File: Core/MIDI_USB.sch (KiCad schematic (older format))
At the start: 27 parts, among them J1 Conn_01x04, J4 Conn_01x06, SW1 SW_Push_DPDT, U1 ATSAMD21G17D-A, U10 TLE9250V, U9 MCP2517FD-xSL, Y1 20MHz

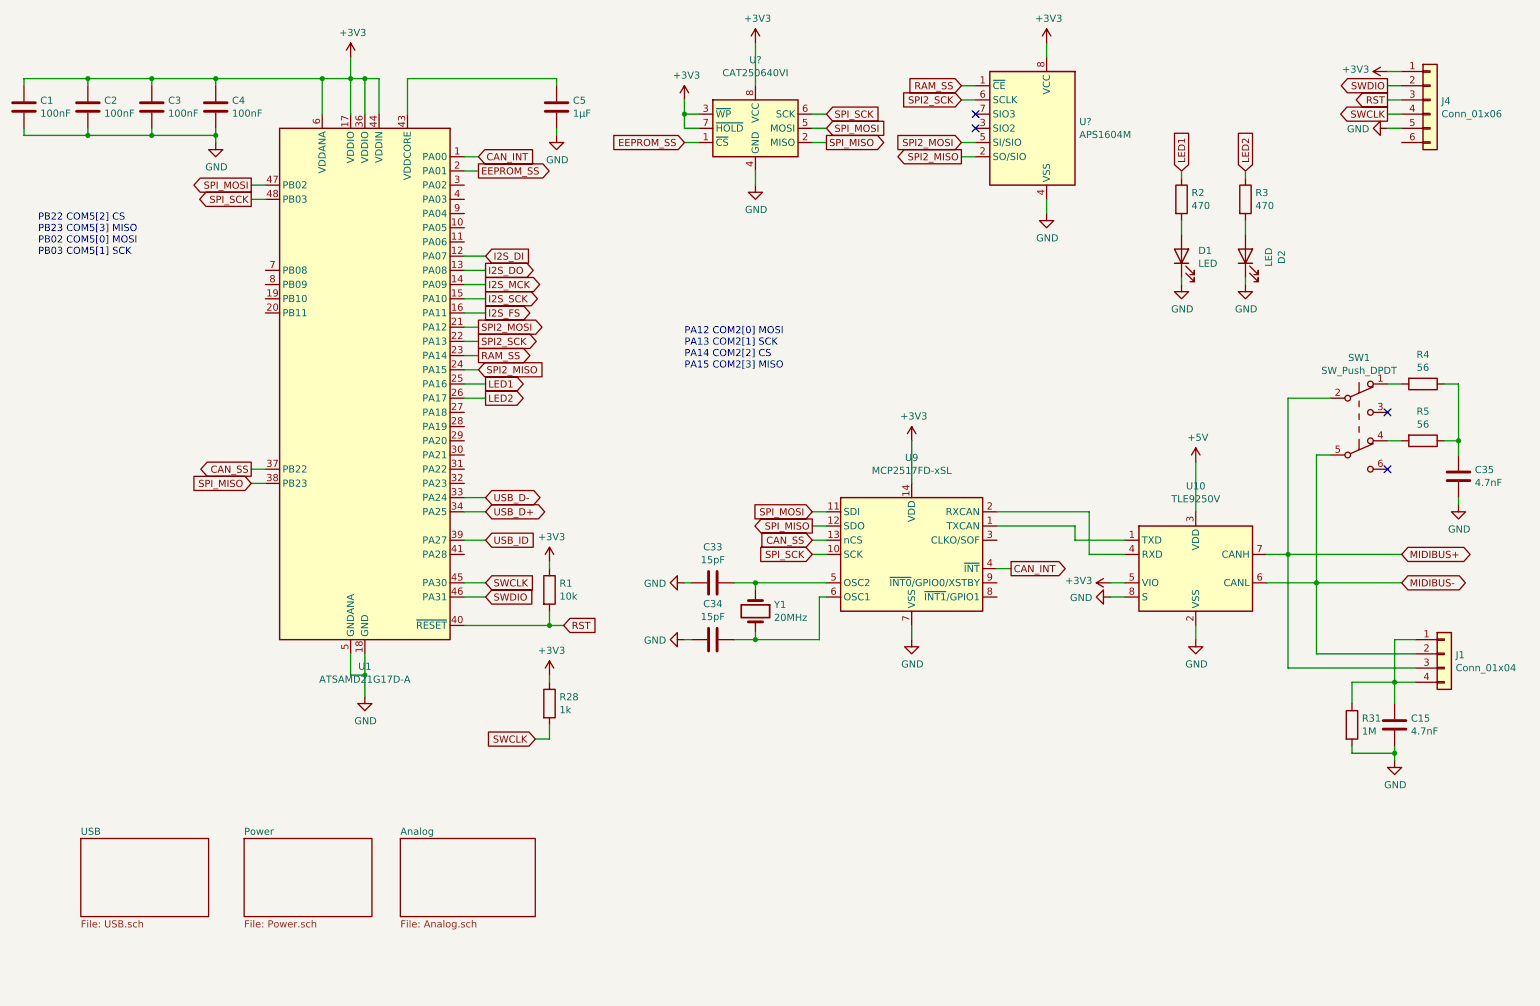
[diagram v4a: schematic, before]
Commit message: Add IO and bootloader buttons
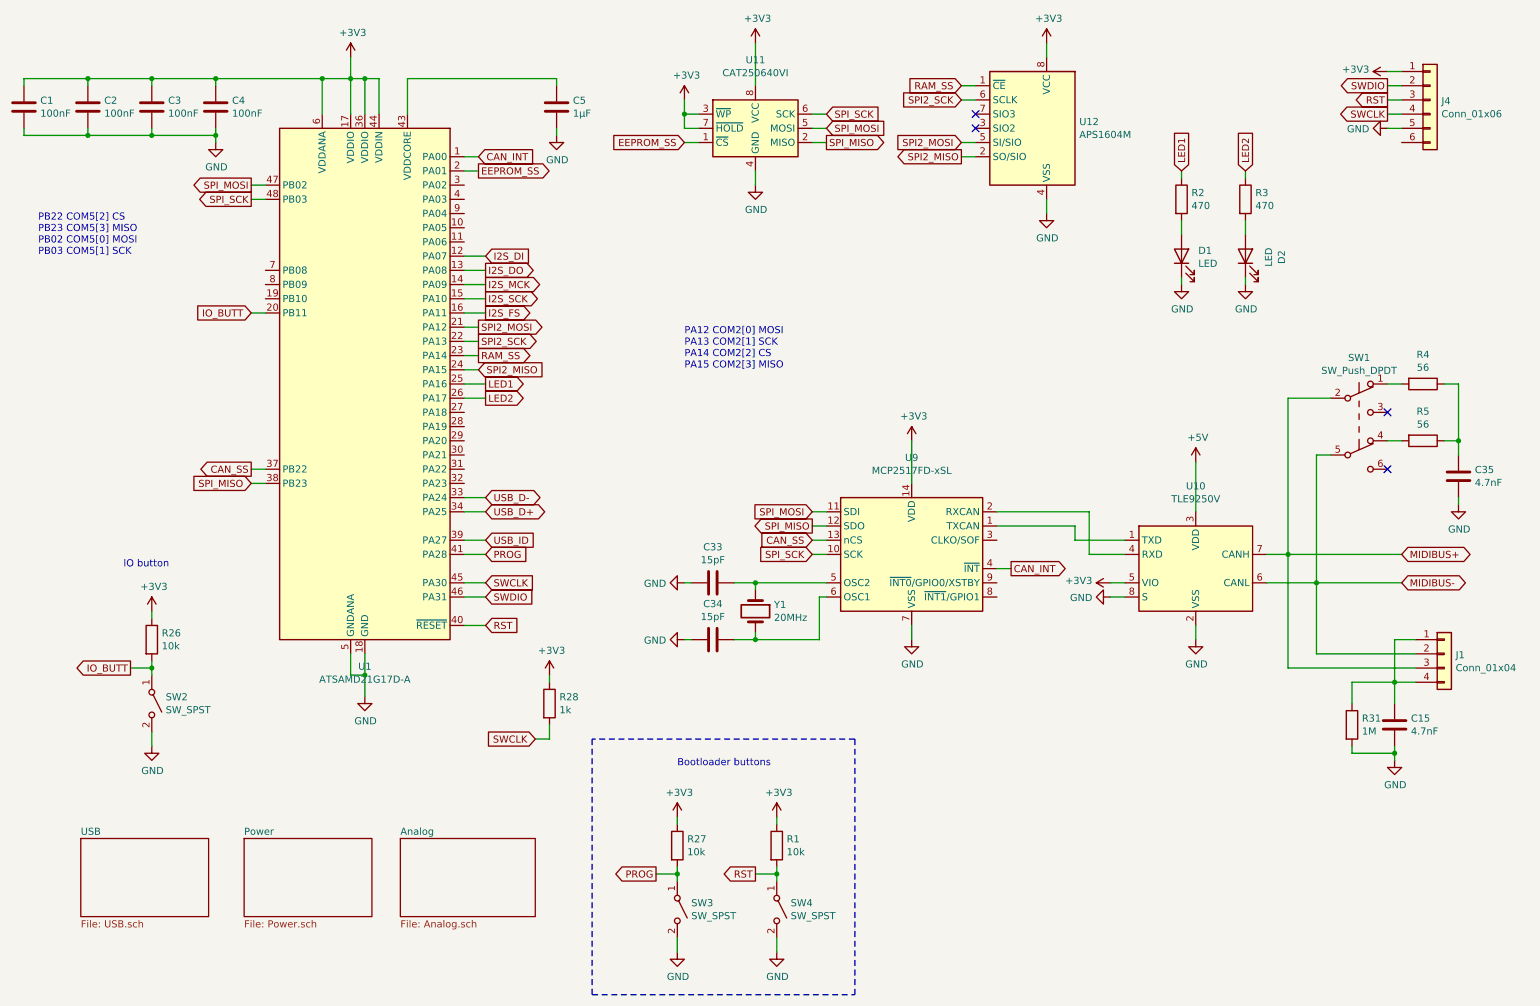
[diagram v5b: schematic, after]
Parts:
- added R26, R27: 10k, Resistor_SMD:R_0603_1608Metric, symbol Device:R
- added SW2: SW_SPST, Button_Switch_THT:SW_Tactile_SPST_Angled_PTS645Vx58-2LFS, symbol Switch:SW_SPST
- added SW3, SW4: SW_SPST, Button_Switch_SMD:SW_SPST_EVQP7C, symbol Switch:SW_SPST
- gave numbers to parts that had none: 2
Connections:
- net +3V3: now also R26.1, R27.1
- net GND: now also SW2.2 (B), SW3.2 (B), SW4.2 (B)
- net RST: now also SW4.1 (A)
- net IO_BUTT: now reaches U1.20 (PB11)
- net IO_BUTT: now also R26.2, SW2.1 (A)
- net PROG: now reaches U1.41 (PA28)
- net PROG: now also R27.2, SW3.1 (A)
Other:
- note added: "Bootloader buttons"
- note added: "IO button"
- moved on the sheet: R1
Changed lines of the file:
@@
 L Device:R R1
 U 1 1 60AB5ED7
-P 4300 4650
-F 0 "R1" H 4370 4696 50  0000 L CNN
-F 1 "10k" H 4370 4605 50  0000 L CNN
-F 2 "Resistor_SMD:R_0603_1608Metric" V 4230 4650 50  0001 C CNN
-F 3 "~" H 4300 4650 50  0001 C CNN
-	1    4300 4650
-	1    0    0    -1
-$EndComp
-Text GLabel 4400 4900 2    50   Input ~ 0
+P 5900 6450
+F 0 "R1" H 5970 6496 50  0000 L CNN
+F 1 "10k" H 5970 6405 50  0000 L CNN
+F 2 "Resistor_SMD:R_0603_1608Metric" V 5830 6450 50  0001 C CNN
+F 3 "~" H 5900 6450 50  0001 C CNN
+	1    5900 6450
+	1    0    0    -1
+$EndComp
+Text GLabel 3850 4900 2    50   Input ~ 0
 RST
 Wire Wire Line
-	4400 4900 4300 4900
-Wire Wire Line
-	4300 4800 4300 4900
-Connection ~ 4300 4900
-Wire Wire Line
-	4300 4900 3700 4900
-Wire Wire Line
-	4300 4500 4300 4450
+	3850 4900 3700 4900
+Wire Wire Line
+	5900 6600 5900 6650
+Wire Wire Line
+	5900 6300 5900 6250
 $Comp
 L power:+3V3 #PWR0110
 U 1 1 60ABC9C1
-P 4300 4450
-F 0 "#PWR0110" H 4300 4300 50  0001 C CNN
-F 1 "+3V3" H 4315 4623 50  0000 C CNN
-F 2 "" H 4300 4450 50  0001 C CNN
-F 3 "" H 4300 4450 50  0001 C CNN
-	1    4300 4450
+P 5900 6250
+F 0 "#PWR0110" H 5900 6100 50  0001 C CNN
+F 1 "+3V3" H 5915 6423 50  0000 C CNN
+F 2 "" H 5900 6250 50  0001 C CNN
+F 3 "" H 5900 6250 50  0001 C CNN
+	1    5900 6250
 	1    0    0    -1
 $EndComp
@@
 SWCLK
 $Comp
-L Memory_EEPROM:CAT250xxx U?
+L Memory_EEPROM:CAT250xxx U11
 U 1 1 62CF50E4
 P 5750 1400
-F 0 "U?" H 5750 1881 50  0000 C CNN
+F 0 "U11" H 5750 1881 50  0000 C CNN
 F 1 "CAT250640VI" H 5750 1790 50  0000 C CNN
 F 2 "Package_SO:SOIC-8_3.9x4.9mm_P1.27mm" H 5750 1400 50  0001 C CNN
@@
 $EndComp
 $Comp
-L Memory_RAM:ESP-PSRAM32 U?
+L Memory_RAM:ESP-PSRAM32 U12
 U 1 1 62CFA564
 P 7700 1400
-F 0 "U?" H 7370 1446 50  0000 R CNN
+F 0 "U12" H 7370 1446 50  0000 R CNN
 F 1 "APS1604M" H 7370 1355 50  0000 R CNN
 F 2 "Package_SO:SOIC-8_3.9x4.9mm_P1.27mm" H 7700 800 50  0001 C CNN
@@
 $EndComp
 $Comp
-L power:+3V3 #PWR?
+L power:+3V3 #PWR0138
 U 1 1 62D0BAED
 P 7800 800
-F 0 "#PWR?" H 7800 650 50  0001 C CNN
+F 0 "#PWR0138" H 7800 650 50  0001 C CNN
 F 1 "+3V3" H 7815 973 50  0000 C CNN
 F 2 "" H 7800 800 50  0001 C CNN
@@
 $EndComp
 $Comp
-L power:+3V3 #PWR?
+L power:+3V3 #PWR0163
 U 1 1 62D0BCD9
 P 5750 800
-F 0 "#PWR?" H 5750 650 50  0001 C CNN
+F 0 "#PWR0163" H 5750 650 50  0001 C CNN
 F 1 "+3V3" H 5765 973 50  0000 C CNN
 F 2 "" H 5750 800 50  0001 C CNN
@@
 	5750 1800 5750 1700
 $Comp
-L power:GND #PWR?
+L power:GND #PWR0165
 U 1 1 62D21FFD
 P 5750 1800
-F 0 "#PWR?" H 5750 1550 50  0001 C CNN
+F 0 "#PWR0165" H 5750 1550 50  0001 C CNN
 F 1 "GND" H 5755 1627 50  0000 C CNN
 F 2 "" H 5750 1800 50  0001 C CNN
@@
 $EndComp
 $Comp
-L power:GND #PWR?
+L power:GND #PWR0196
 U 1 1 62D228FF
 P 7800 2000
-F 0 "#PWR?" H 7800 1750 50  0001 C CNN
+F 0 "#PWR0196" H 7800 1750 50  0001 C CNN
 F 1 "GND" H 7805 1827 50  0000 C CNN
 F 2 "" H 7800 2000 50  0001 C CNN
@@
 	7200 1100 7300 1100
 $Comp
-L power:+3V3 #PWR?
+L power:+3V3 #PWR0197
 U 1 1 62D75718
 P 5250 1200
-F 0 "#PWR?" H 5250 1050 50  0001 C CNN
+F 0 "#PWR0197" H 5250 1050 50  0001 C CNN
 F 1 "+3V3" H 5265 1373 50  0000 C CNN
 F 2 "" H 5250 1200 50  0001 C CNN
@@
 Text Notes 5250 3100 0    50   ~ 0
 PA12 COM2[0] MOSI\nPA13 COM2[1] SCK\nPA14 COM2[2] CS\nPA15 COM2[3] MISO
+$Comp
+L Device:R R27
+U 1 1 62DDAB41
+P 5200 6450
+F 0 "R27" H 5270 6496 50  0000 L CNN
+F 1 "10k" H 5270 6405 50  0000 L CNN
+F 2 "Resistor_SMD:R_0603_1608Metric" V 5130 6450 50  0001 C CNN
+F 3 "~" H 5200 6450 50  0001 C CNN
+	1    5200 6450
+	1    0    0    -1
+$EndComp
+Wire Wire Line
+	5200 6600 5200 6650
+Wire Wire Line
+	5200 6300 5200 6250
+$Comp
+L power:+3V3 #PWR0206
+U 1 1 62DDAF8B
+P 5200 6250
+F 0 "#PWR0206" H 5200 6100 50  0001 C CNN
+F 1 "+3V3" H 5215 6423 50  0000 C CNN
+F 2 "" H 5200 6250 50  0001 C CNN
+F 3 "" H 5200 6250 50  0001 C CNN
+	1    5200 6250
+	1    0    0    -1
+$EndComp
+Text GLabel 3850 4400 2    50   Input ~ 0
+PROG
+Wire Wire Line
+	3850 4400 3700 4400
+$Comp
+L Switch:SW_SPST SW3
+U 1 1 62E052F7
+P 5200 6900
+F 0 "SW3" V 5154 6998 50  0000 L CNN
+F 1 "SW_SPST" V 5245 6998 50  0000 L CNN
+F 2 "Button_Switch_SMD:SW_SPST_EVQP7C" H 5200 6900 50  0001 C CNN
+F 3 "~" H 5200 6900 50  0001 C CNN
+	1    5200 6900
+	0    1    1    0
+$EndComp
+$Comp
+L Switch:SW_SPST SW4
+U 1 1 62E06963
+P 5900 6900
+F 0 "SW4" V 5854 6998 50  0000 L CNN
+F 1 "SW_SPST" V 5945 6998 50  0000 L CNN
+F 2 "Button_Switch_SMD:SW_SPST_EVQP7C" H 5900 6900 50  0001 C CNN
+F 3 "~" H 5900 6900 50  0001 C CNN
+	1    5900 6900
+	0    1    1    0
+$EndComp
+Text GLabel 5750 6650 0    50   Output ~ 0
+RST
+Text GLabel 5050 6650 0    50   Output ~ 0
+PROG
+Wire Wire Line
+	5050 6650 5200 6650
+Connection ~ 5200 6650
+Wire Wire Line
+	5200 6650 5200 6700
+Wire Wire Line
+	5750 6650 5900 6650
+Connection ~ 5900 6650
+Wire Wire Line
+	5900 6650 5900 6700
+Wire Wire Line
+	5900 7200 5900 7100
+Wire Wire Line
+	5200 7200 5200 7100
+$Comp
+L power:GND #PWR0207
+U 1 1 62E213B4
+P 5900 7200
+F 0 "#PWR0207" H 5900 6950 50  0001 C CNN
+F 1 "GND" H 5905 7027 50  0000 C CNN
+F 2 "" H 5900 7200 50  0001 C CNN
+F 3 "" H 5900 7200 50  0001 C CNN
+	1    5900 7200
+	1    0    0    -1
+$EndComp
+$Comp
+L power:GND #PWR0208
+U 1 1 62E2221F
+P 5200 7200
+F 0 "#PWR0208" H 5200 6950 50  0001 C CNN
+F 1 "GND" H 5205 7027 50  0000 C CNN
+F 2 "" H 5200 7200 50  0001 C CNN
+F 3 "" H 5200 7200 50  0001 C CNN
+	1    5200 7200
+	1    0    0    -1
+$EndComp
+Text Notes 5200 5900 0    50   ~ 0
+Bootloader buttons
+Wire Notes Line
+	6450 7500 6450 5700
+Wire Notes Line
+	6450 5700 4600 5700
+Wire Notes Line
+	4600 5700 4600 7500
+Wire Notes Line
+	4600 7500 6450 7500
+$Comp
+L Device:R R26
+U 1 1 62E3FA14
+P 1500 5000
+F 0 "R26" H 1570 5046 50  0000 L CNN
+F 1 "10k" H 1570 4955 50  0000 L CNN
+F 2 "Resistor_SMD:R_0603_1608Metric" V 1430 5000 50  0001 C CNN
+F 3 "~" H 1500 5000 50  0001 C CNN
+	1    1500 5000
+	1    0    0    -1
+$EndComp
+Wire Wire Line
+	1500 5150 1500 5200
+Wire Wire Line
+	1500 4850 1500 4800
+$Comp
+L power:+3V3 #PWR0209
+U 1 1 62E3FEC0
+P 1500 4800
+F 0 "#PWR0209" H 1500 4650 50  0001 C CNN
+F 1 "+3V3" H 1515 4973 50  0000 C CNN
+F 2 "" H 1500 4800 50  0001 C CNN
+F 3 "" H 1500 4800 50  0001 C CNN
+	1    1500 4800
+	1    0    0    -1
+$EndComp
+$Comp
+L Switch:SW_SPST SW2
+U 1 1 62E3FECA
+P 1500 5450
+F 0 "SW2" V 1454 5548 50  0000 L CNN
+F 1 "SW_SPST" V 1545 5548 50  0000 L CNN
+F 2 "Button_Switch_THT:SW_Tactile_SPST_Angled_PTS645Vx58-2LFS" H 1500 5450 50  0001 C CNN
+F 3 "~" H 1500 5450 50  0001 C CNN
+	1    1500 5450
+	0    1    1    0
+$EndComp
+Wire Wire Line
+	1350 5200 1500 5200
+Connection ~ 1500 5200
+Wire Wire Line
+	1500 5200 1500 5250
+Wire Wire Line
+	1500 5750 1500 5650
+$Comp
+L power:GND #PWR0210
+U 1 1 62E3FED8
+P 1500 5750
+F 0 "#PWR0210" H 1500 5500 50  0001 C CNN
+F 1 "GND" H 1505 5577 50  0000 C CNN
+F 2 "" H 1500 5750 50  0001 C CNN
+F 3 "" H 1500 5750 50  0001 C CNN
+	1    1500 5750
+	1    0    0    -1
+$EndComp
+Text Notes 1300 4500 0    50   ~ 0
+IO button
+Text GLabel 1350 5200 0    50   Output ~ 0
+IO_BUTT
+Text GLabel 2200 2700 0    50   Input ~ 0
+IO_BUTT
+Wire Wire Line
+	2200 2700 2300 2700
 $EndSCHEMATC

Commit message: Add external RTC oscillator
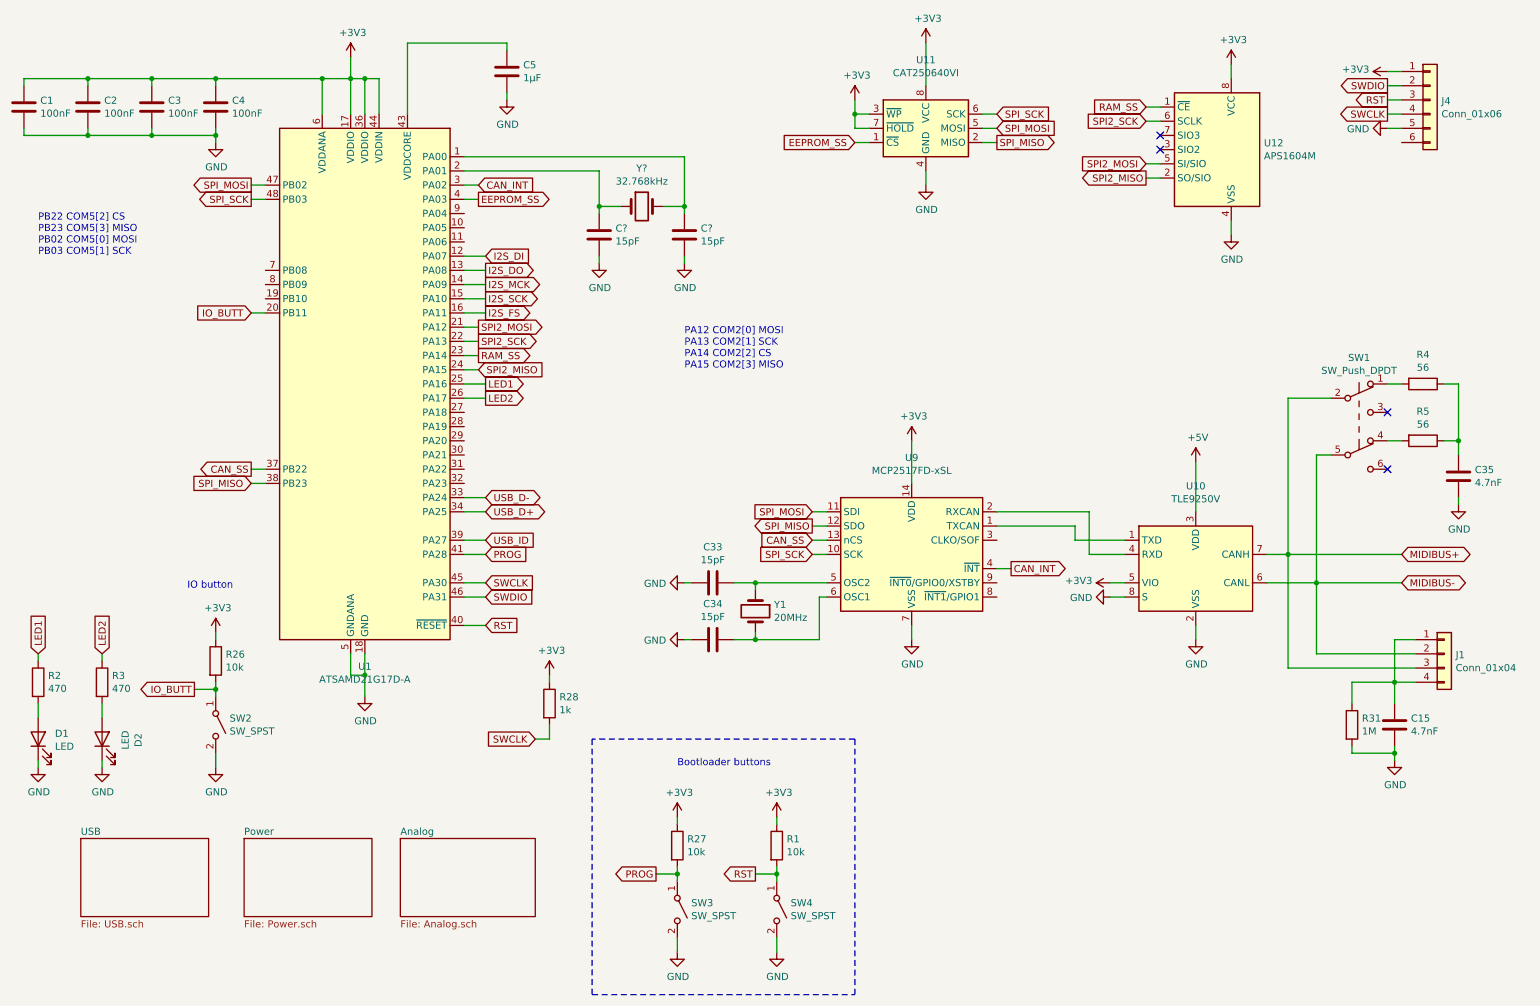
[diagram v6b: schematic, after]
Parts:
- added C? (x2): 15pF, Capacitor_SMD:C_0603_1608Metric, symbol Device:C
- added Y?: 32.768kHz, Crystal:Crystal_SMD_EuroQuartz_EQ161-2Pin_3.2x1.5mm_HandSoldering, symbol Device:Crystal
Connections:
- net CAN_INT: now also U1.3 (PA02); no longer U1.1 (PA00)
- net EEPROM_SS: now also U1.4 (PA03); no longer U1.2 (PA01)
- net GND: now also C?.2, C?.2
- new net: C?.1, U1.1 (PA00), Y?.2
- new net: C?.1, U1.2 (PA01), Y?.1
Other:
- moved on the sheet: C5, D1, D2, R2, R26, R3, SW2, U11, U12
